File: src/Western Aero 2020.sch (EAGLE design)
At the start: 94 parts, among them IC1 LT1963AET, IC2 LT1963AET, J1 PITOT, J10 ANA_IO, J11 PWR, J12 POWER, J2 BUZZER, J3 RX2/TX2, J4 RX3/TX3, J5 SPI, J6 DIG_IO, J7 RX1/TX1, J8 DIG_IO, J9 REF/GND, U3 TEENSY_3.5_DIL+4, U5 SPARKFUN_MPU9250_IMU, U6 ADAFRUIT_MPL3115A2_BAROMETER, U7 ADAFRUIT_INA219_BATTERY_SENSOR, U8 ADAFRUIT_RFM95W_LORA_RADIO, U9 ADAFRUIT_MTK3339_GPS

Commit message: Finished new route.
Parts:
- removed J12: POWER, SparkFun-Connectors:CONN_02
- added BAT_GND, BAT_VIN: (no value), SparkFun-Connectors:CONN_01
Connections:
- net GND: now also BAT_GND.1; no longer J12.1
- net VIN+: now also BAT_VIN.1; no longer J12.2
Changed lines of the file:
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@@
 <part name="7805" library="SparkFun-IC-Power" library_urn="urn:adsk.eagle:library:526" deviceset="V_REG_78XX" device="SINK" package3d_urn="urn:adsk.eagle:package:39063/1" value="7805"/>
 <part name="J5" library="SparkFun-Connectors" library_urn="urn:adsk.eagle:library:513" deviceset="CONN_04" device="" package3d_urn="urn:adsk.eagle:package:38085/1" value="SPI"/>
-<part name="J12" library="SparkFun-Connectors" library_urn="urn:adsk.eagle:library:513" deviceset="CONN_02" device="" package3d_urn="urn:adsk.eagle:package:38039/1" value="POWER"/>
 <part name="IC1" library="linear-technology" library_urn="urn:adsk.eagle:library:261" deviceset="LT1963AET*" device="" package3d_urn="urn:adsk.eagle:package:16056/1"/>
 <part name="IC2" library="linear-technology" library_urn="urn:adsk.eagle:library:261" deviceset="LT1963AET*" device="" package3d_urn="urn:adsk.eagle:package:16056/1"/>
@@
 <part name="SDA" library="SparkFun-Connectors" library_urn="urn:adsk.eagle:library:513" deviceset="CONN_01" device="" package3d_urn="urn:adsk.eagle:package:38028/1"/>
 <part name="3.3V" library="SparkFun-Connectors" library_urn="urn:adsk.eagle:library:513" deviceset="CONN_01" device="" package3d_urn="urn:adsk.eagle:package:38028/1"/>
+<part name="BAT_GND" library="SparkFun-Connectors" library_urn="urn:adsk.eagle:library:513" deviceset="CONN_01" device="" package3d_urn="urn:adsk.eagle:package:38028/1"/>
+<part name="BAT_VIN" library="SparkFun-Connectors" library_urn="urn:adsk.eagle:library:513" deviceset="CONN_01" device="" package3d_urn="urn:adsk.eagle:package:38028/1"/>
 </parts>
 <sheets>
@@
 <attribute name="NAME" x="5.588" y="223.52" size="1.778" layer="95" font="vector" rot="R270"/>
 </instance>
-<instance part="J12" gate="G$1" x="-40.64" y="57.912" smashed="yes" rot="R270">
-<attribute name="VALUE" x="-45.466" y="60.452" size="1.778" layer="96" font="vector" rot="R270"/>
-<attribute name="NAME" x="-35.052" y="60.452" size="1.778" layer="95" font="vector" rot="R270"/>
-</instance>
 <instance part="IC1" gate="G$1" x="-66.04" y="12.7" smashed="yes" rot="R180">
 <attribute name="NAME" x="-58.42" y="6.35" size="1.778" layer="95" rot="R180"/>
@@
 <attribute name="VALUE" x="56.134" y="180.34" size="1.778" layer="96" font="vector" rot="R270"/>
 <attribute name="NAME" x="64.008" y="180.34" size="1.778" layer="95" font="vector" rot="R270"/>
+</instance>
+<instance part="BAT_GND" gate="G$1" x="-45.72" y="58.42" smashed="yes" rot="R270">
+<attribute name="VALUE" x="-50.546" y="60.96" size="1.778" layer="96" font="vector" rot="R270"/>
+<attribute name="NAME" x="-42.672" y="60.96" size="1.778" layer="95" font="vector" rot="R270"/>
+</instance>
+<instance part="BAT_VIN" gate="G$1" x="-33.02" y="58.42" smashed="yes" rot="R270">
+<attribute name="VALUE" x="-37.846" y="60.96" size="1.778" layer="96" font="vector" rot="R270"/>
+<attribute name="NAME" x="-29.972" y="60.96" size="1.778" layer="95" font="vector" rot="R270"/>
 </instance>
 </instances>
@@
 <segment>
 <label x="-38.1" y="35.56" size="1.778" layer="95"/>
-<wire x1="-38.1" y1="50.292" x2="-38.1" y2="43.18" width="0.1524" layer="91"/>
-<pinref part="J12" gate="G$1" pin="2"/>
 <pinref part="BAT" gate="G$1" pin="1"/>
 <wire x1="-38.1" y1="43.18" x2="-38.1" y2="35.56" width="0.1524" layer="91"/>
 <wire x1="-33.02" y1="43.18" x2="-38.1" y2="43.18" width="0.1524" layer="91"/>
+<pinref part="BAT_VIN" gate="G$1" pin="1"/>
+<wire x1="-33.02" y1="50.8" x2="-38.1" y2="50.8" width="0.1524" layer="91"/>
+<wire x1="-38.1" y1="50.8" x2="-38.1" y2="43.18" width="0.1524" layer="91"/>
 <junction x="-38.1" y="43.18"/>
 </segment>
@@
 <segment>
 <label x="-45.72" y="35.56" size="1.778" layer="95"/>
-<pinref part="J12" gate="G$1" pin="1"/>
-<wire x1="-40.64" y1="50.292" x2="-40.64" y2="43.18" width="0.1524" layer="91"/>
 <pinref part="GND" gate="G$1" pin="1"/>
 <wire x1="-40.64" y1="43.18" x2="-40.64" y2="35.56" width="0.1524" layer="91"/>
 <wire x1="-45.72" y1="43.18" x2="-40.64" y2="43.18" width="0.1524" layer="91"/>
+<pinref part="BAT_GND" gate="G$1" pin="1"/>
+<wire x1="-45.72" y1="50.8" x2="-40.64" y2="50.8" width="0.1524" layer="91"/>
+<wire x1="-40.64" y1="43.18" x2="-40.64" y2="50.8" width="0.1524" layer="91"/>
 <junction x="-40.64" y="43.18"/>
 </segment>

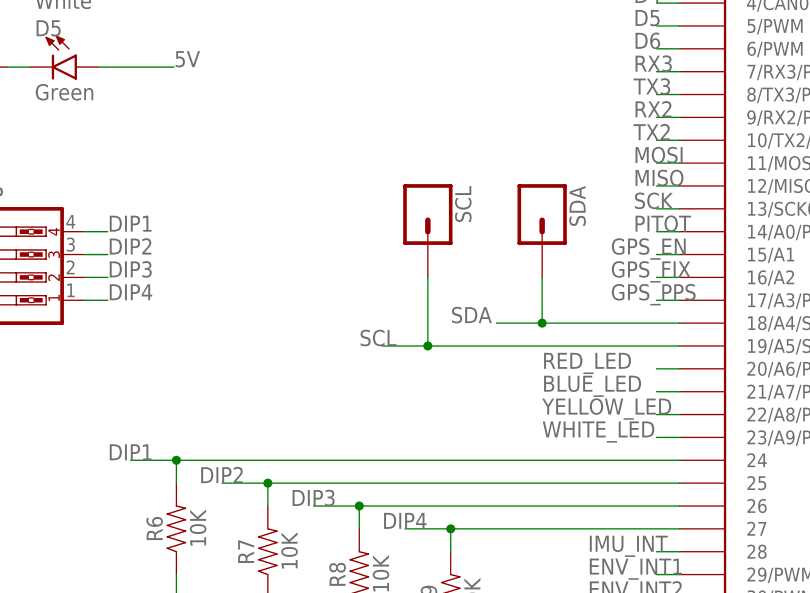
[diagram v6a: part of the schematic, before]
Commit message: Trace adjustments
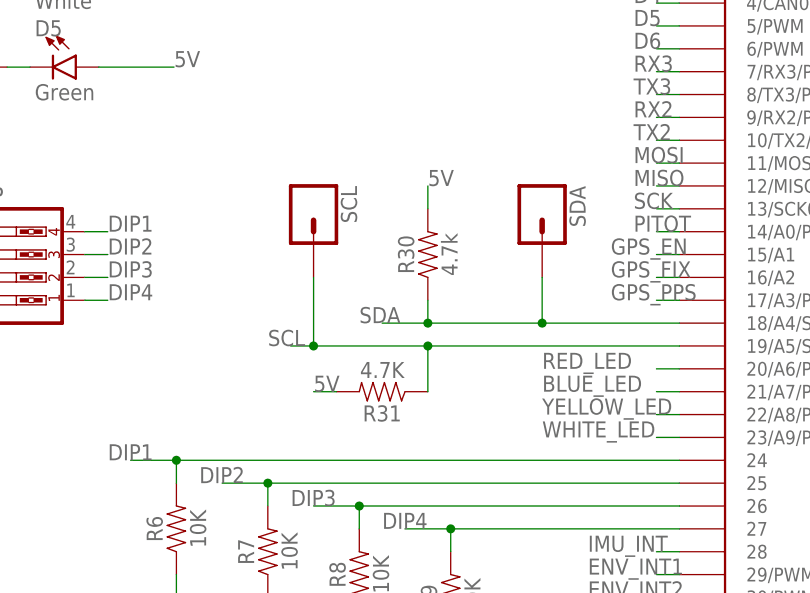
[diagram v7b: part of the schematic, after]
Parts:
- added R30: 4.7k, SparkFun-Resistors:330OHM-HORIZ-1/10W-5%
- added R31: 4.7K, SparkFun-Resistors:330OHM-HORIZ-1/10W-5%
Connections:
- net 5V: now also R30.2, R31.2
- net SCL: now also R31.1
- net SDA: now also R30.1
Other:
- moved on the sheet: SCL
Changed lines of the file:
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@@
 <part name="BAT_GND" library="SparkFun-Connectors" library_urn="urn:adsk.eagle:library:513" deviceset="CONN_01" device="" package3d_urn="urn:adsk.eagle:package:38028/1"/>
 <part name="BAT_VIN" library="SparkFun-Connectors" library_urn="urn:adsk.eagle:library:513" deviceset="CONN_01" device="" package3d_urn="urn:adsk.eagle:package:38028/1"/>
+<part name="R30" library="SparkFun-Resistors" library_urn="urn:adsk.eagle:library:532" deviceset="330OHM" device="-HORIZ-1/10W-5%" package3d_urn="urn:adsk.eagle:package:39658/1" value="4.7k"/>
+<part name="R31" library="SparkFun-Resistors" library_urn="urn:adsk.eagle:library:532" deviceset="330OHM" device="-HORIZ-1/10W-5%" package3d_urn="urn:adsk.eagle:package:39658/1" value="4.7K"/>
 </parts>
 <sheets>
@@
 <attribute name="NAME" x="-104.14" y="-2.032" size="1.778" layer="95" font="vector"/>
 </instance>
-<instance part="SCL" gate="G$1" x="-27.94" y="137.16" smashed="yes" rot="R270">
-<attribute name="VALUE" x="-32.766" y="139.7" size="1.778" layer="96" font="vector" rot="R270"/>
-<attribute name="NAME" x="-24.892" y="139.7" size="1.778" layer="95" font="vector" rot="R270"/>
+<instance part="SCL" gate="G$1" x="-40.64" y="137.16" smashed="yes" rot="R270">
+<attribute name="VALUE" x="-45.466" y="139.7" size="1.778" layer="96" font="vector" rot="R270"/>
+<attribute name="NAME" x="-37.592" y="139.7" size="1.778" layer="95" font="vector" rot="R270"/>
 </instance>
 <instance part="SDA" gate="G$1" x="-15.24" y="137.16" smashed="yes" rot="R270">
@@
 <attribute name="VALUE" x="-37.846" y="60.96" size="1.778" layer="96" font="vector" rot="R270"/>
 <attribute name="NAME" x="-29.972" y="60.96" size="1.778" layer="95" font="vector" rot="R270"/>
+</instance>
+<instance part="R30" gate="G$1" x="-27.94" y="132.08" smashed="yes" rot="R90">
+<attribute name="NAME" x="-29.464" y="132.08" size="1.778" layer="95" font="vector" rot="R90" align="bottom-center"/>
+<attribute name="VALUE" x="-26.416" y="132.08" size="1.778" layer="96" font="vector" rot="R90" align="top-center"/>
+</instance>
+<instance part="R31" gate="G$1" x="-33.02" y="116.84" smashed="yes" rot="R180">
+<attribute name="NAME" x="-33.02" y="115.316" size="1.778" layer="95" font="vector" rot="R180" align="bottom-center"/>
+<attribute name="VALUE" x="-33.02" y="118.364" size="1.778" layer="96" font="vector" rot="R180" align="top-center"/>
 </instance>
 </instances>
@@
 <pinref part="U3" gate="G$1" pin="18/A4/SDA0"/>
 <wire x1="0" y1="124.46" x2="-15.24" y2="124.46" width="0.1524" layer="91"/>
-<label x="-25.4" y="124.46" size="1.778" layer="95"/>
+<label x="-35.56" y="124.46" size="1.778" layer="95"/>
 <pinref part="SDA" gate="G$1" pin="1"/>
-<wire x1="-15.24" y1="124.46" x2="-20.32" y2="124.46" width="0.1524" layer="91"/>
+<wire x1="-15.24" y1="124.46" x2="-27.94" y2="124.46" width="0.1524" layer="91"/>
+<wire x1="-27.94" y1="124.46" x2="-33.02" y2="124.46" width="0.1524" layer="91"/>
 <wire x1="-15.24" y1="129.54" x2="-15.24" y2="124.46" width="0.1524" layer="91"/>
 <junction x="-15.24" y="124.46"/>
+<wire x1="-27.94" y1="124.46" x2="-27.94" y2="127" width="0.1524" layer="91"/>
+<junction x="-27.94" y="124.46"/>
+<pinref part="R30" gate="G$1" pin="1"/>
 </segment>
 </net>
@@
 <pinref part="U3" gate="G$1" pin="19/A5/SCL0"/>
 <wire x1="0" y1="121.92" x2="-27.94" y2="121.92" width="0.1524" layer="91"/>
-<label x="-35.56" y="121.92" size="1.778" layer="95"/>
+<label x="-45.72" y="121.92" size="1.778" layer="95"/>
 <pinref part="SCL" gate="G$1" pin="1"/>
-<wire x1="-27.94" y1="121.92" x2="-33.02" y2="121.92" width="0.1524" layer="91"/>
-<wire x1="-27.94" y1="129.54" x2="-27.94" y2="121.92" width="0.1524" layer="91"/>
+<wire x1="-27.94" y1="121.92" x2="-40.64" y2="121.92" width="0.1524" layer="91"/>
+<wire x1="-40.64" y1="121.92" x2="-43.18" y2="121.92" width="0.1524" layer="91"/>
+<wire x1="-40.64" y1="129.54" x2="-40.64" y2="121.92" width="0.1524" layer="91"/>
+<junction x="-40.64" y="121.92"/>
 <junction x="-27.94" y="121.92"/>
+<pinref part="R31" gate="G$1" pin="1"/>
+<wire x1="-27.94" y1="121.92" x2="-27.94" y2="116.84" width="0.1524" layer="91"/>
 </segment>
 </net>
@@
 <label x="25.4" y="10.16" size="1.778" layer="95"/>
 </segment>
+<segment>
+<pinref part="R31" gate="G$1" pin="2"/>
+<wire x1="-38.1" y1="116.84" x2="-40.64" y2="116.84" width="0.1524" layer="91"/>
+<label x="-40.64" y="116.84" size="1.778" layer="95"/>
+</segment>
+<segment>
+<pinref part="R30" gate="G$1" pin="2"/>
+<wire x1="-27.94" y1="137.16" x2="-27.94" y2="139.7" width="0.1524" layer="91"/>
+<label x="-27.94" y="139.7" size="1.778" layer="95"/>
+</segment>
 </net>

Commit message: Trace rework
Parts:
- J8: device SparkFun-Connectors:CONN_04 -> SparkFun-Connectors:CONN_05
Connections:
- removed net CS: J5.4, U3.33/A14/TX5, U8.CS
- new net D33: J8.5, U3.33/A14/TX5
- new net TX_2: J5.4, U8.CS
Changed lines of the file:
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@@
 <part name="J9" library="SparkFun-Connectors" library_urn="urn:adsk.eagle:library:513" deviceset="CONN_02" device="" package3d_urn="urn:adsk.eagle:package:38039/1" value="REF/GND"/>
 <part name="J11" library="SparkFun-Connectors" library_urn="urn:adsk.eagle:library:513" deviceset="CONN_04" device="" package3d_urn="urn:adsk.eagle:package:38085/1" value="PWR"/>
-<part name="J8" library="SparkFun-Connectors" library_urn="urn:adsk.eagle:library:513" deviceset="CONN_04" device="" package3d_urn="urn:adsk.eagle:package:38085/1" value="DIG_IO"/>
 <part name="R1" library="SparkFun-Resistors" library_urn="urn:adsk.eagle:library:532" deviceset="330OHM" device="-HORIZ-1/10W-5%" package3d_urn="urn:adsk.eagle:package:39658/1" value="220"/>
 <part name="R2" library="SparkFun-Resistors" library_urn="urn:adsk.eagle:library:532" deviceset="330OHM" device="-HORIZ-1/10W-5%" package3d_urn="urn:adsk.eagle:package:39658/1" value="220"/>
@@
 <part name="R30" library="SparkFun-Resistors" library_urn="urn:adsk.eagle:library:532" deviceset="330OHM" device="-HORIZ-1/10W-5%" package3d_urn="urn:adsk.eagle:package:39658/1" value="4.7k"/>
 <part name="R31" library="SparkFun-Resistors" library_urn="urn:adsk.eagle:library:532" deviceset="330OHM" device="-HORIZ-1/10W-5%" package3d_urn="urn:adsk.eagle:package:39658/1" value="4.7K"/>
+<part name="J8" library="SparkFun-Connectors" library_urn="urn:adsk.eagle:library:513" deviceset="CONN_05" device="" package3d_urn="urn:adsk.eagle:package:38104/1" value="DIG_IO"/>
 </parts>
 <sheets>
@@
 <attribute name="NAME" x="56.388" y="200.66" size="1.778" layer="95" font="vector" rot="R270"/>
 </instance>
-<instance part="J8" gate="G$1" x="22.86" y="195.58" smashed="yes" rot="R270">
-<attribute name="VALUE" x="15.494" y="200.66" size="1.778" layer="96" font="vector" rot="R270"/>
-<attribute name="NAME" x="30.988" y="200.66" size="1.778" layer="95" font="vector" rot="R270"/>
-</instance>
 <instance part="R1" gate="G$1" x="-79.756" y="193.548" smashed="yes">
 <attribute name="NAME" x="-79.756" y="195.072" size="1.778" layer="95" font="vector" align="bottom-center"/>
@@
 <attribute name="NAME" x="-33.02" y="115.316" size="1.778" layer="95" font="vector" rot="R180" align="bottom-center"/>
 <attribute name="VALUE" x="-33.02" y="118.364" size="1.778" layer="96" font="vector" rot="R180" align="top-center"/>
+</instance>
+<instance part="J8" gate="G$1" x="25.4" y="198.12" smashed="yes" rot="R270">
+<attribute name="VALUE" x="15.494" y="200.66" size="1.778" layer="96" font="vector" rot="R270"/>
+<attribute name="NAME" x="33.528" y="200.66" size="1.778" layer="95" font="vector" rot="R270"/>
 </instance>
 </instances>
@@
 <wire x1="0" y1="213.36" x2="0" y2="210.82" width="0.1524" layer="91"/>
 <label x="0" y="210.82" size="1.778" layer="95" rot="R270"/>
-</segment>
-</net>
-<net name="CS" class="0">
-<segment>
-<pinref part="U8" gate="G$1" pin="CS"/>
-<wire x1="116.84" y1="154.94" x2="114.3" y2="154.94" width="0.1524" layer="91"/>
-<label x="111.76" y="154.94" size="1.778" layer="95"/>
-</segment>
-<segment>
-<pinref part="U3" gate="G$1" pin="33/A14/TX5"/>
-<wire x1="0" y1="86.36" x2="-2.54" y2="86.36" width="0.1524" layer="91"/>
-<label x="-10.16" y="86.36" size="1.778" layer="95"/>
-</segment>
-<segment>
-<pinref part="J5" gate="G$1" pin="4"/>
-<wire x1="2.54" y1="213.36" x2="2.54" y2="210.82" width="0.1524" layer="91"/>
-<label x="2.54" y="210.82" size="1.778" layer="95" rot="R270"/>
 </segment>
 </net>
@@
 <net name="D3" class="0">
 <segment>
-<pinref part="J8" gate="G$1" pin="1"/>
 <wire x1="20.32" y1="190.5" x2="20.32" y2="187.96" width="0.1524" layer="91"/>
 <label x="20.32" y="187.96" size="1.778" layer="95" rot="R270"/>
+<pinref part="J8" gate="G$1" pin="1"/>
 </segment>
 <segment>
@@
 <net name="D4" class="0">
 <segment>
-<pinref part="J8" gate="G$1" pin="2"/>
 <wire x1="22.86" y1="190.5" x2="22.86" y2="187.96" width="0.1524" layer="91"/>
 <label x="22.86" y="187.96" size="1.778" layer="95" rot="R270"/>
+<pinref part="J8" gate="G$1" pin="2"/>
 </segment>
 <segment>
@@
 <net name="D5" class="0">
 <segment>
-<pinref part="J8" gate="G$1" pin="3"/>
 <wire x1="25.4" y1="190.5" x2="25.4" y2="187.96" width="0.1524" layer="91"/>
 <label x="25.4" y="187.96" size="1.778" layer="95" rot="R270"/>
+<pinref part="J8" gate="G$1" pin="3"/>
 </segment>
 <segment>
@@
 <net name="D6" class="0">
 <segment>
-<pinref part="J8" gate="G$1" pin="4"/>
 <wire x1="27.94" y1="190.5" x2="27.94" y2="187.96" width="0.1524" layer="91"/>
 <label x="27.94" y="187.96" size="1.778" layer="95" rot="R270"/>
+<pinref part="J8" gate="G$1" pin="4"/>
 </segment>
 <segment>
@@
 <label x="185.42" y="0" size="1.778" layer="95"/>
 <wire x1="200.66" y1="0" x2="190.5" y2="0" width="0.1524" layer="91"/>
+</segment>
+</net>
+<net name="TX_2" class="0">
+<segment>
+<pinref part="U8" gate="G$1" pin="CS"/>
+<wire x1="116.84" y1="154.94" x2="114.3" y2="154.94" width="0.1524" layer="91"/>
+<label x="109.22" y="154.94" size="1.778" layer="95"/>
+</segment>
+<segment>
+<pinref part="J5" gate="G$1" pin="4"/>
+<wire x1="2.54" y1="213.36" x2="2.54" y2="210.82" width="0.1524" layer="91"/>
+<label x="2.54" y="210.82" size="1.778" layer="95" rot="R270"/>
+</segment>
+</net>
+<net name="D33" class="0">
+<segment>
+<pinref part="U3" gate="G$1" pin="33/A14/TX5"/>
+<wire x1="0" y1="86.36" x2="-2.54" y2="86.36" width="0.1524" layer="91"/>
+<label x="-5.08" y="86.36" size="1.778" layer="95"/>
+</segment>
+<segment>
+<pinref part="J8" gate="G$1" pin="5"/>
+<wire x1="30.48" y1="190.5" x2="30.48" y2="187.96" width="0.1524" layer="91"/>
+<label x="30.48" y="187.96" size="1.778" layer="95" rot="R90" align="top-right"/>
 </segment>
 </net>
@@
 packages will not be understood (or retained) with this version.
 </note>
+<note version="9.0" severity="warning">
+Since Version 9.0, EAGLE supports the align property for labels.
+Labels in schematic will not be understood with this version. Update EAGLE to the latest version
+for full support of labels.
+</note>
 </compatibility>
